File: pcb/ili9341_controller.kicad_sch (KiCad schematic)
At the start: 87 parts, among them J1 USB_B_Micro, J2 RP_SWD_CONN, J3 CONN_RP2040, J4 CONN_FPGA, J5 CONN_TFT, Q1 NPN, Q2 NPN, Q3 NPN, SW1 RP_RST_SW, SW2 RP_USB_BOOT_SW, U1 ICE40UP5K-SG48ITR, U2 LM3880, U3 TLV75512PDBV, U4 TLV75525PDBV, U5 TLV75533PDBV, U6 RP2040, U7 W25Q128JVS, Y1 12MHz

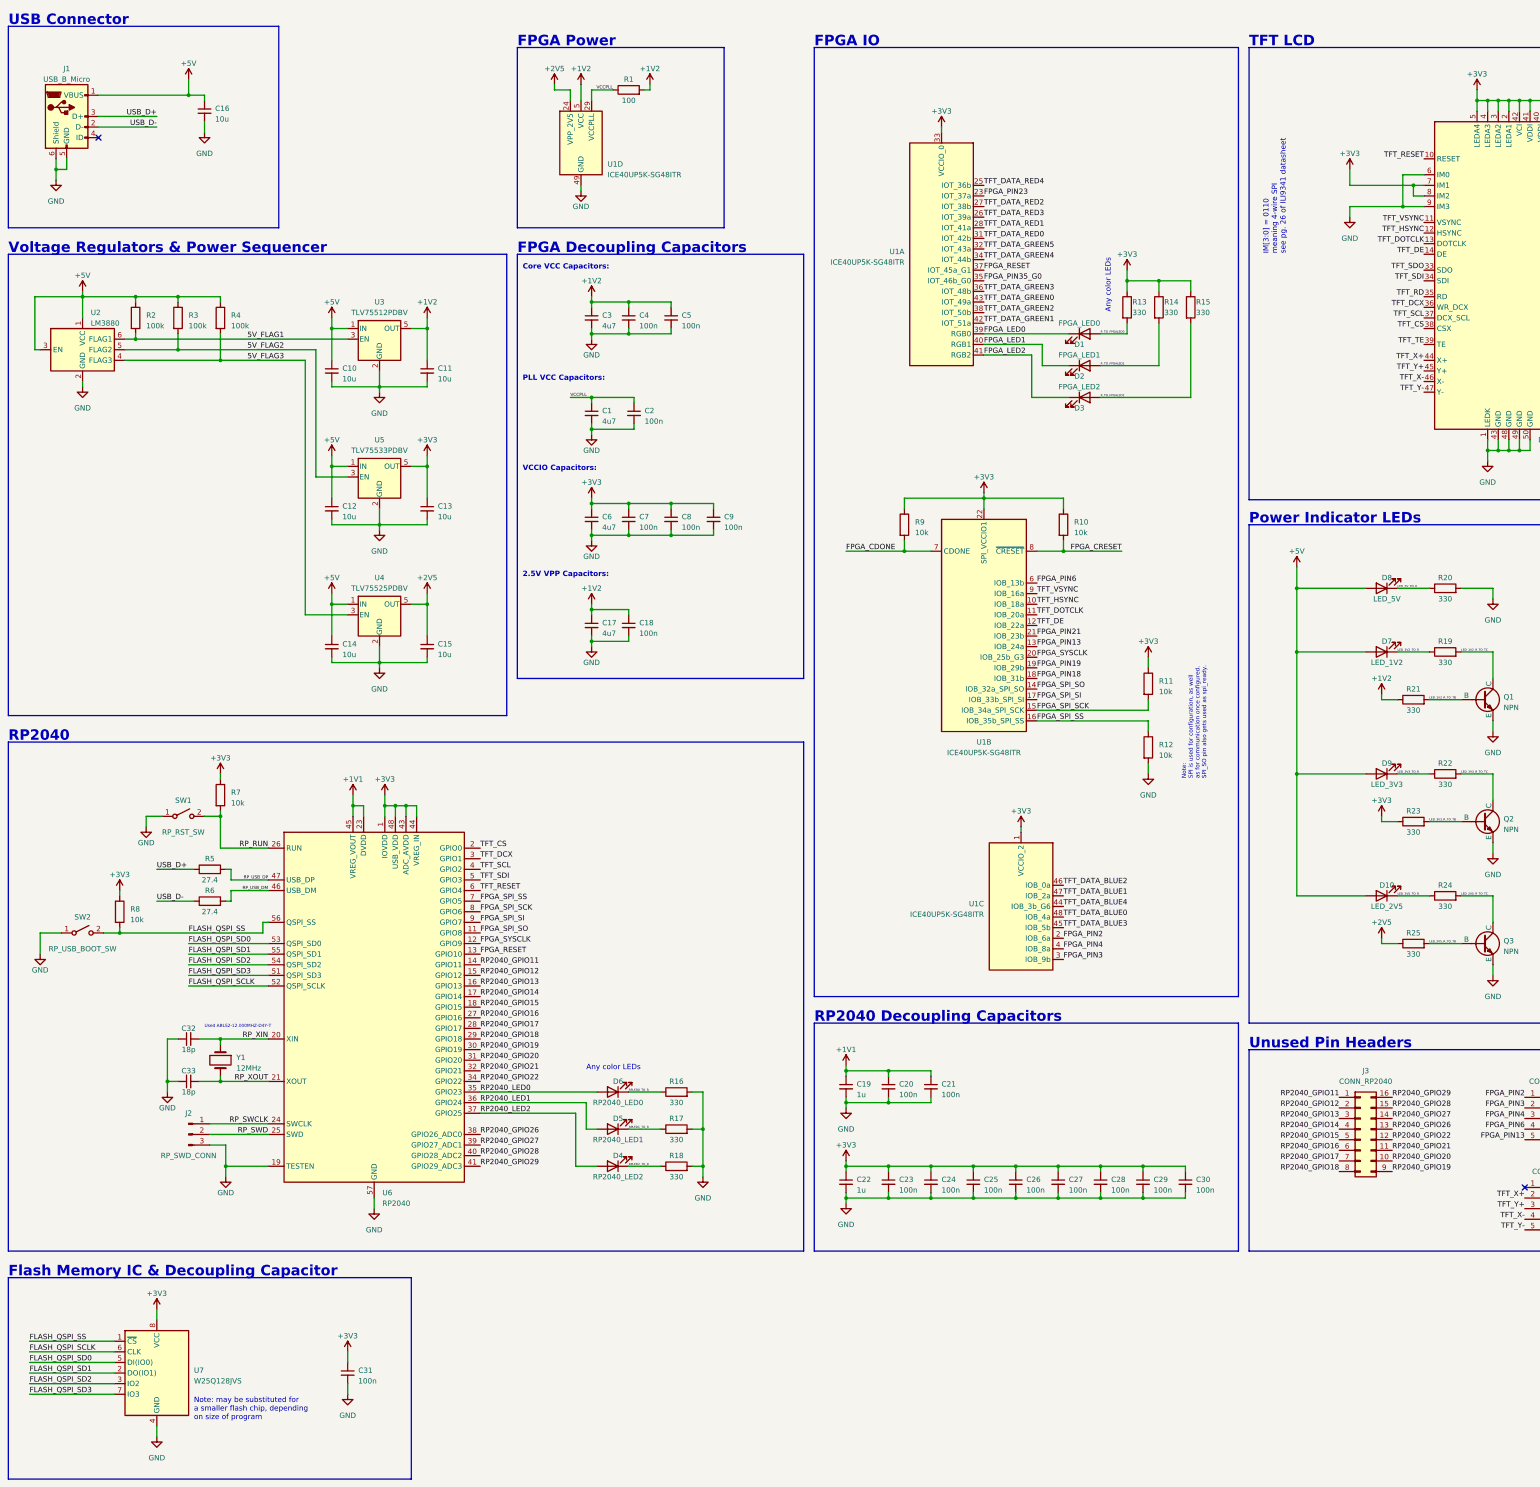
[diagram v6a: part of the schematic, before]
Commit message: add test points to all unexposed pins
also connected CRESET and CDONE to the RP2040, since i apparently forgot to do that
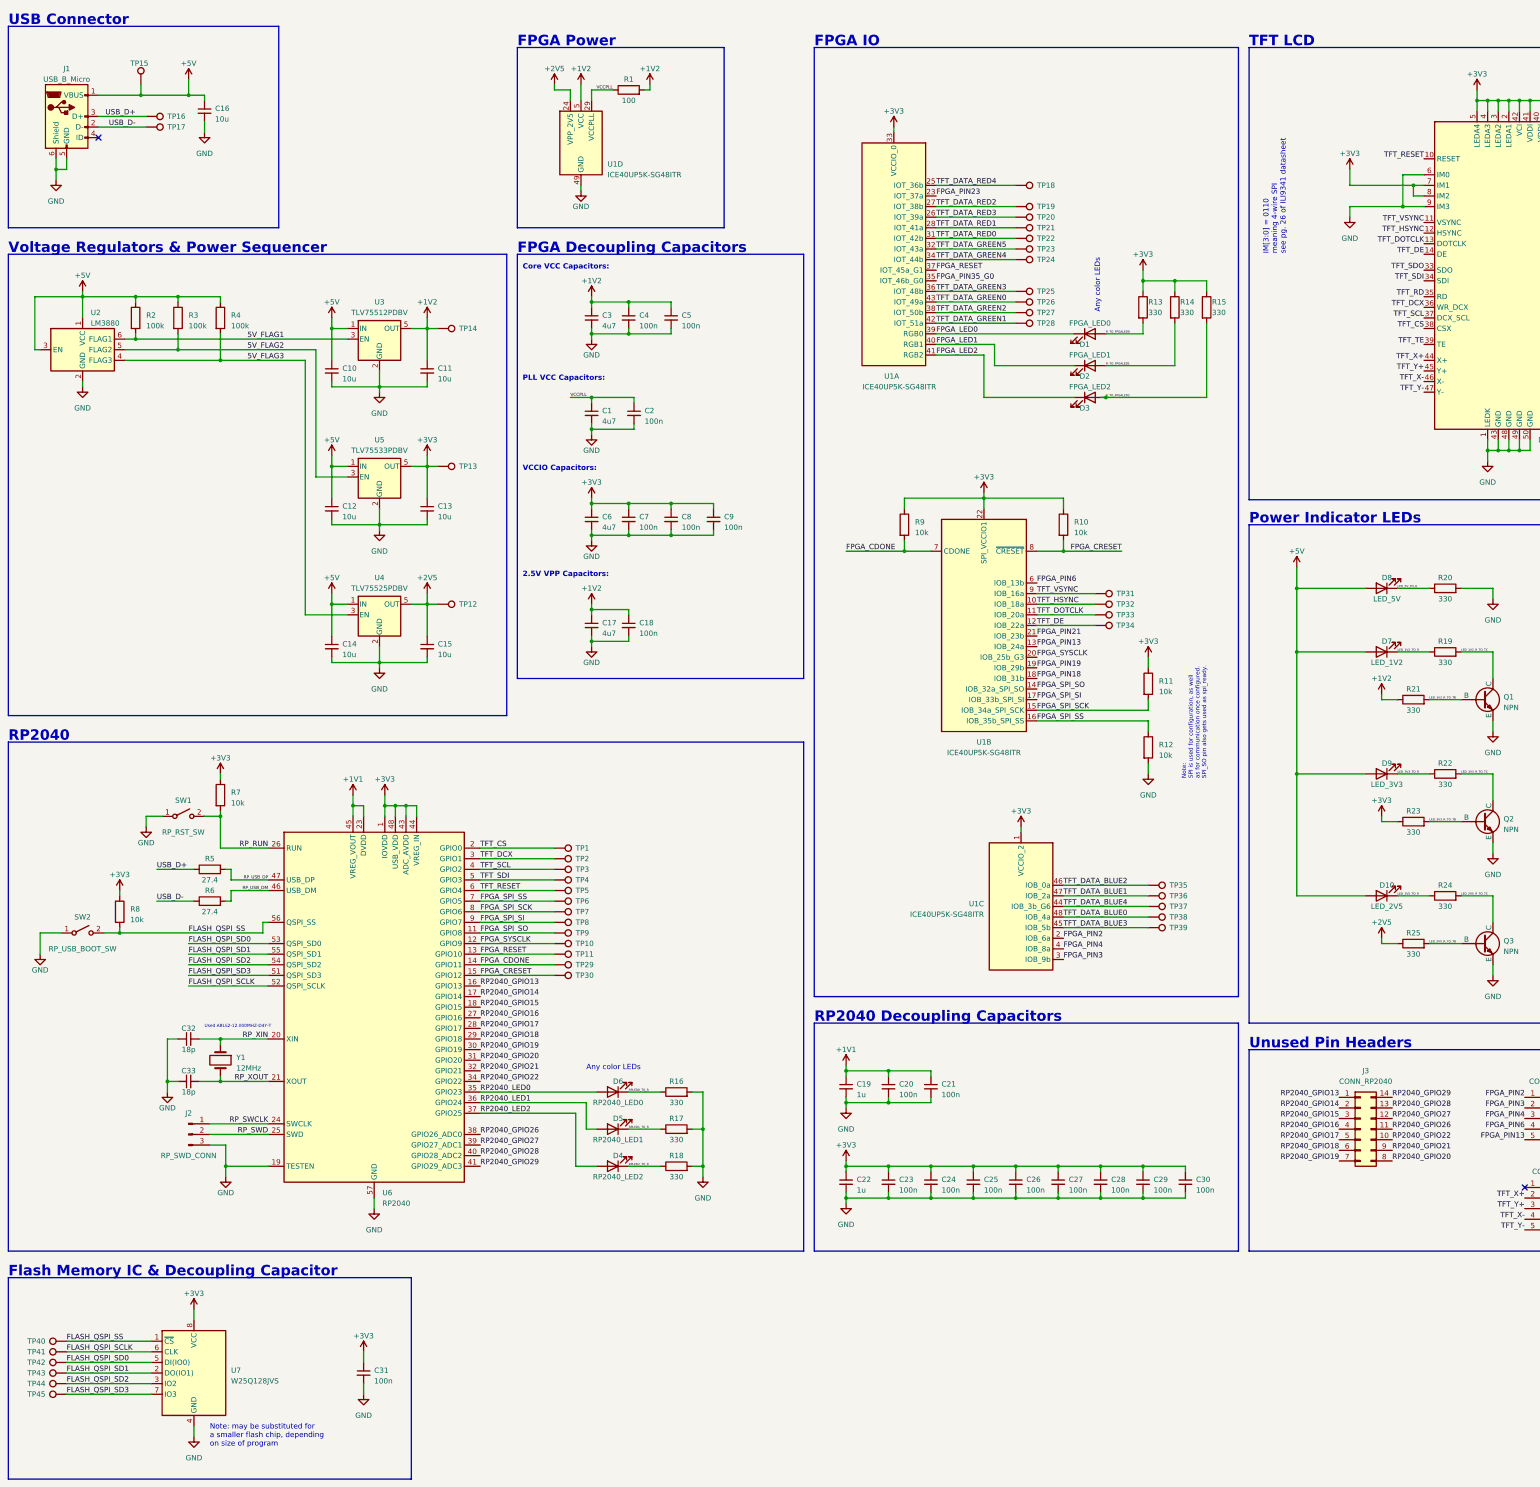
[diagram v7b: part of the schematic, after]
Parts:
- removed J3: CONN_RP2040, symbol Connector_Generic:Conn_02x08_Counter_Clockwise
- added J3: CONN_RP2040, symbol Connector_Generic:Conn_02x07_Counter_Clockwise
- added TP1, TP10, TP11, TP12, TP13, TP14, TP15, TP16, TP17, TP18, TP19, TP2, TP20, TP21, TP22, TP23, TP24, TP25, TP26, TP27, TP28, TP29, TP3, TP30, TP31, TP32, TP33, TP34, TP35, TP36, TP37, TP38, TP39, TP4, TP40, TP41, TP42, TP43, TP44, TP45, TP5, TP6, TP7, TP8, TP9: TestPoint, symbol Connector:TestPoint
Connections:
- net RP2040_GPIO11 is gone; now on net FPGA_CDONE: U6.14 (GPIO11)
- net RP2040_GPIO12 is gone; now on net FPGA_CRESET: U6.15 (GPIO12)
- net +1V2: now also TP14.1
- net +2V5: now also TP12.1
- net +3V3: now also TP13.1
- net +5V: now also TP15.1
- net FLASH_QSPI_SCLK: now also TP41.1
- net FLASH_QSPI_SD0: now also TP42.1
- net FLASH_QSPI_SD1: now also TP43.1
- net FLASH_QSPI_SD2: now also TP44.1
- net FLASH_QSPI_SD3: now also TP45.1
- net FLASH_QSPI_SS: now also TP40.1
- net FPGA_CDONE: now also TP29.1
- net FPGA_CRESET: now also TP30.1
- net FPGA_RESET: now also TP11.1
- net FPGA_SPI_SCK: now also TP7.1
- net FPGA_SPI_SI: now also TP8.1
- net FPGA_SPI_SO: now also TP9.1
- net FPGA_SPI_SS: now also TP6.1
- net FPGA_SYSCLK: now also TP10.1
- net RP2040_GPIO13: now also J3.1 (Pin_1)
- net RP2040_GPIO14: now also J3.2 (Pin_2)
- net RP2040_GPIO15: now also J3.3 (Pin_3)
- net RP2040_GPIO16: now also J3.4 (Pin_4)
- net RP2040_GPIO17: now also J3.5 (Pin_5)
- net RP2040_GPIO18: now also J3.6 (Pin_6)
- net RP2040_GPIO19: now also J3.7 (Pin_7)
- net RP2040_GPIO20: now also J3.8 (Pin_8)
- net RP2040_GPIO21: now also J3.9 (Pin_9)
- net RP2040_GPIO22: now also J3.10 (Pin_10)
- net RP2040_GPIO26: now also J3.11 (Pin_11)
- net RP2040_GPIO27: now also J3.12 (Pin_12)
- net RP2040_GPIO28: now also J3.13 (Pin_13)
- net RP2040_GPIO29: now also J3.14 (Pin_14)
- net TFT_CS: now also TP1.1
- net TFT_DATA_BLUE0: now also TP38.1
- net TFT_DATA_BLUE1: now also TP36.1
- net TFT_DATA_BLUE2: now also TP35.1
- net TFT_DATA_BLUE3: now also TP39.1
- net TFT_DATA_BLUE4: now also TP37.1
- net TFT_DATA_GREEN0: now also TP26.1
- net TFT_DATA_GREEN1: now also TP28.1
- net TFT_DATA_GREEN2: now also TP27.1
- net TFT_DATA_GREEN3: now also TP25.1
- net TFT_DATA_GREEN4: now also TP24.1
- net TFT_DATA_GREEN5: now also TP23.1
- net TFT_DATA_RED0: now also TP22.1
- net TFT_DATA_RED1: now also TP21.1
- net TFT_DATA_RED2: now also TP19.1
- net TFT_DATA_RED3: now also TP20.1
- net TFT_DATA_RED4: now also TP18.1
- net TFT_DCX: now also TP2.1
- net TFT_DE: now also TP34.1
- net TFT_DOTCLK: now also TP33.1
- net TFT_HSYNC: now also TP32.1
- net TFT_RESET: now also TP5.1
- net TFT_SCL: now also TP3.1
- net TFT_SDI: now also TP4.1
- net TFT_VSYNC: now also TP31.1
- net USB_D+: now also TP16.1
- net USB_D-: now also TP17.1
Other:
- moved on the sheet: C31, D1, D2, D3, R13, R14, R15, U1A, U7

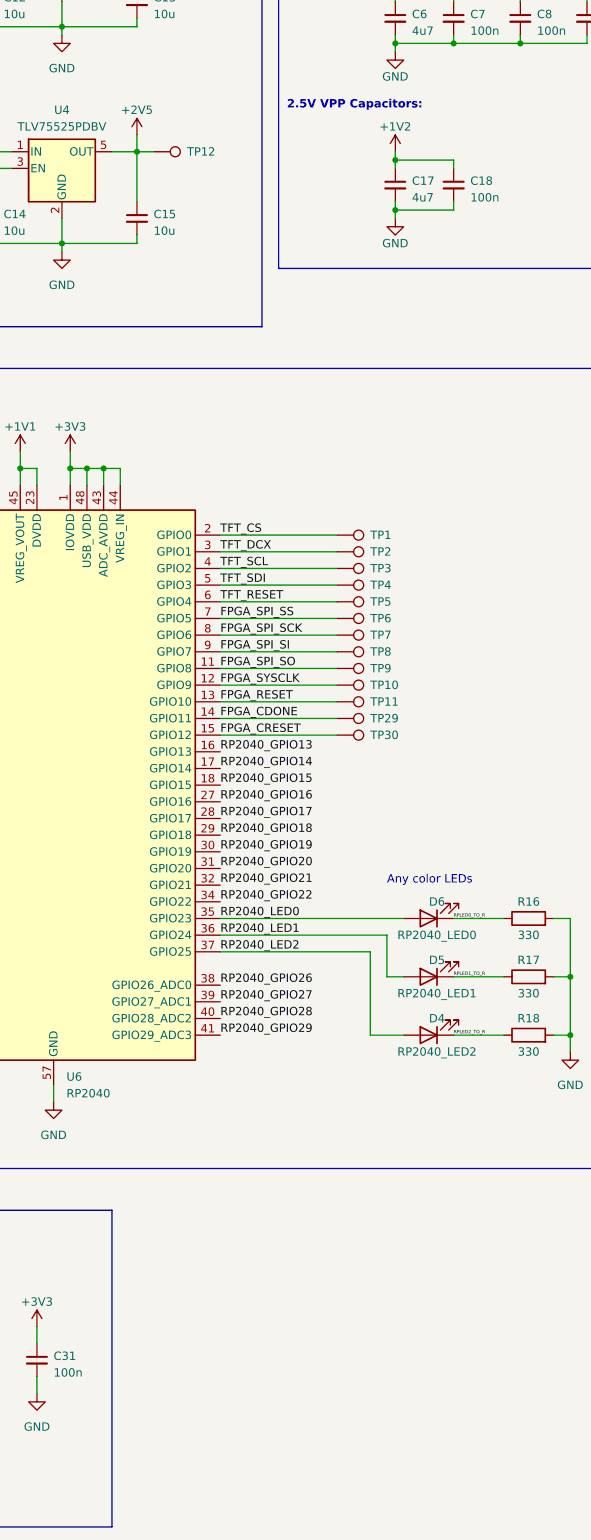
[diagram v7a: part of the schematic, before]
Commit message: add power pin header
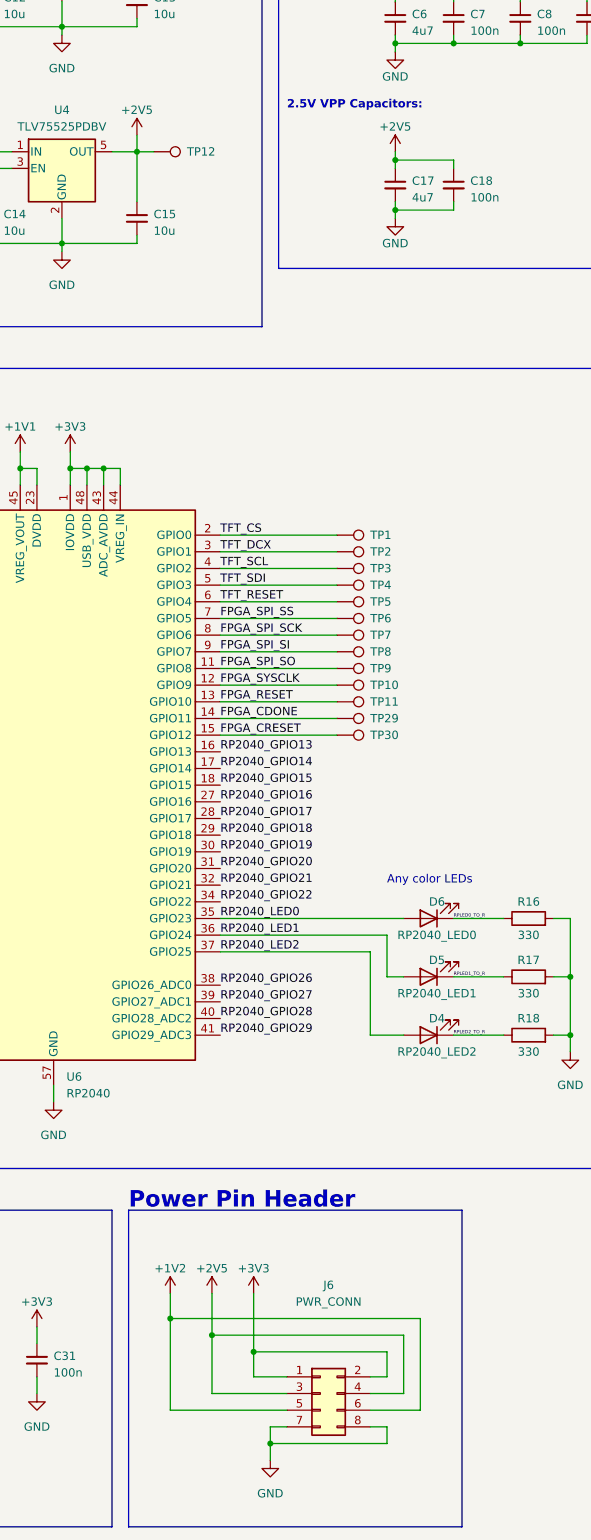
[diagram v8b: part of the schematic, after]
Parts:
- added J6: PWR_CONN, symbol Connector_Generic:Conn_02x04_Odd_Even
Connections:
- net +1V2: now also J6.5 (Pin_5), J6.6 (Pin_6); no longer C17.1, C18.1
- net +2V5: now also C17.1, C18.1, J6.3 (Pin_3), J6.4 (Pin_4)
- net +3V3: now also J6.1 (Pin_1), J6.2 (Pin_2)
- net GND: now also J6.7 (Pin_7), J6.8 (Pin_8)
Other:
- note added: "Power Pin Header"
